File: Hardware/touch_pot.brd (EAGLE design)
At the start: 44.5 x 78.7 mm, 78 parts, among them U1 PIC16F1829, U2 AD5262, U3 5V

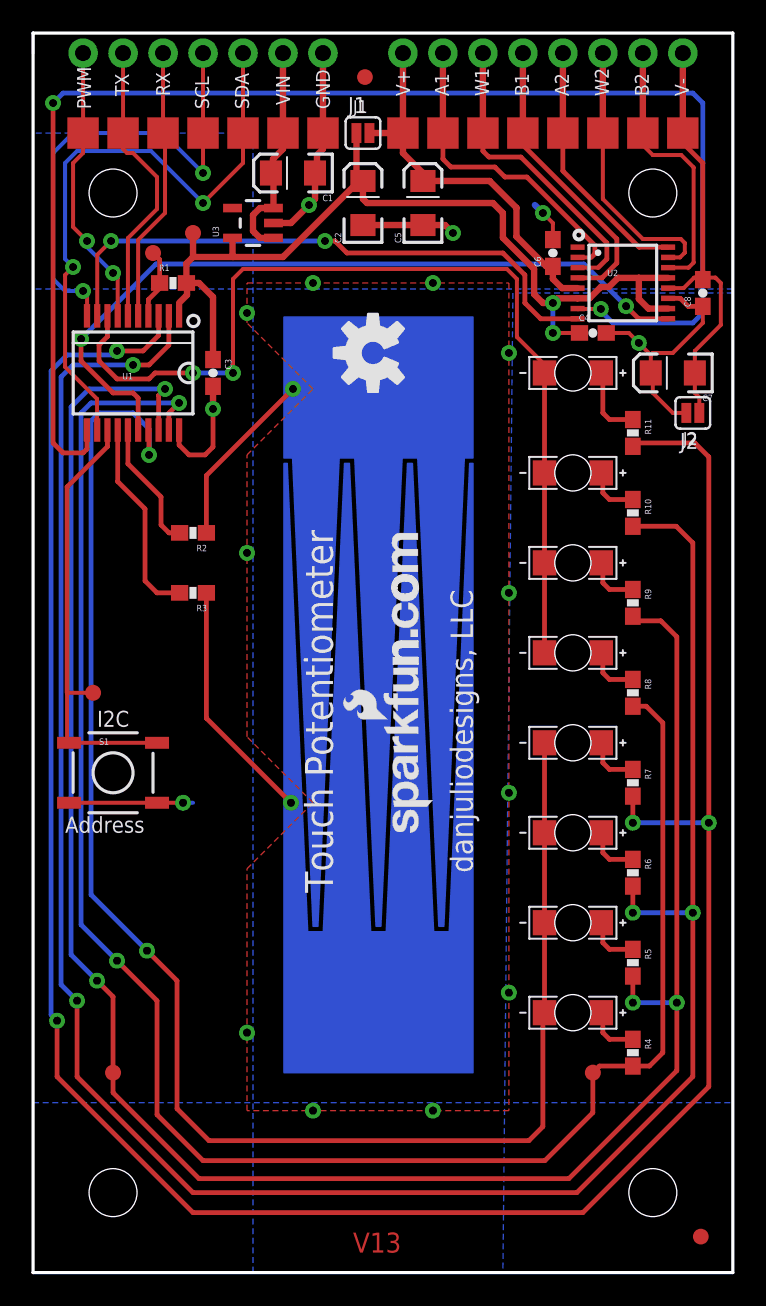
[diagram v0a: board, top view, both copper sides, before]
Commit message: Clean-up, change button text
Moved traces away from hole, deleted unused ground traces, resized one
trace, changed button text for both i2c and cal.
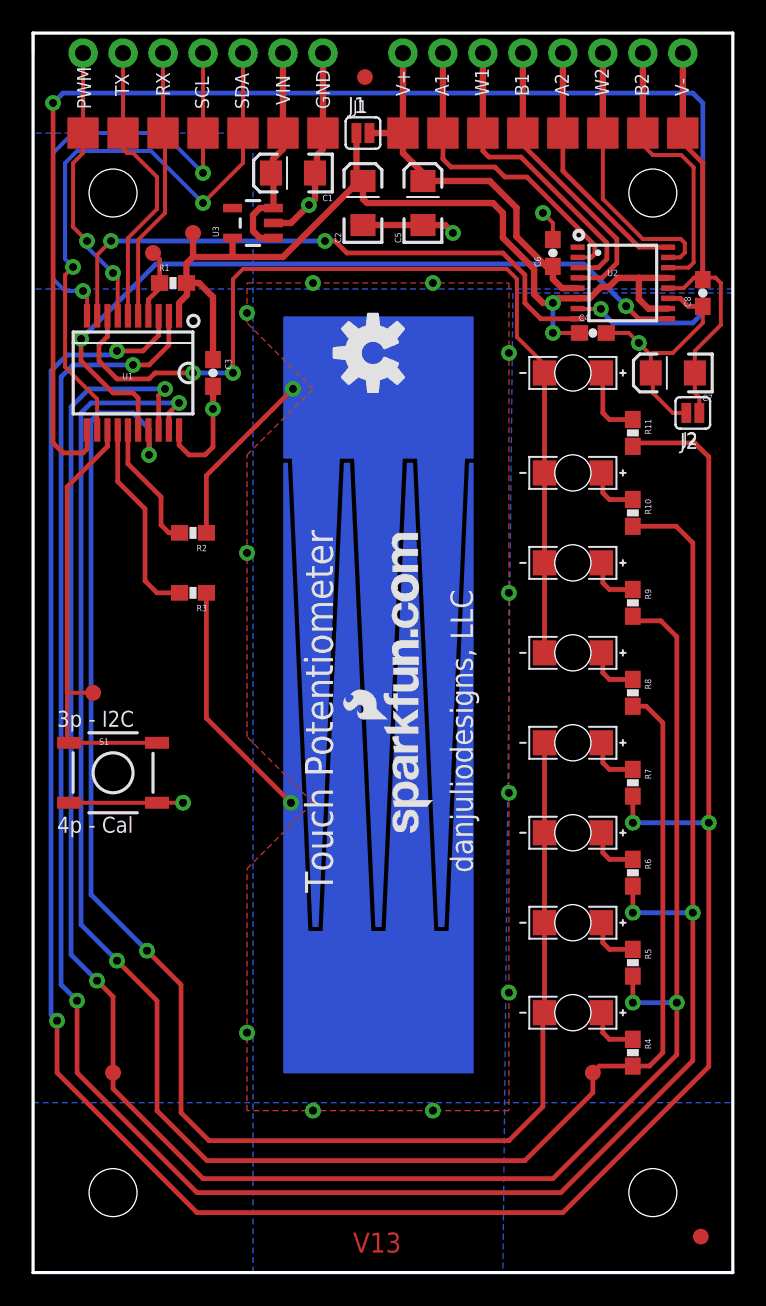
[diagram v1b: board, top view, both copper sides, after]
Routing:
- net GND: track 52.9 -> 51.6 mm
- net LA3: track 154.1 -> 153.2 mm
- net LA0: track 116.0 -> 115.1 mm
- net LA1: track 130.2 -> 129.5 mm
- net LED_PWM1: track 102.4 -> 101.6 mm
- net LA2: track 143.3 -> 142.5 mm
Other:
- board text added: "3p - I2C"
- board text added: "4p - Cal"
- board text removed: "Address"
- board text removed: "I2C"
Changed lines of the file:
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@@
 <text x="53.34" y="-16.51" size="1.778" layer="51" font="vector" ratio="10">danjuliodesigns, LLC</text>
 <text x="20.32" y="1.27" size="1.27" layer="1" font="vector" ratio="15" distance="45">V13</text>
-<text x="4.064" y="34.671" size="1.016" layer="21" font="vector" ratio="15">I2C</text>
-<text x="2.032" y="27.94" size="1.016" layer="21" font="vector" ratio="15">Address</text>
+<text x="1.524" y="34.671" size="1.016" layer="21" font="vector" ratio="15">3p - I2C</text>
+<text x="1.524" y="27.94" size="1.016" layer="21" font="vector" ratio="15">4p - Cal</text>
 <text x="20.32" y="73.66" size="0.8128" layer="21" font="vector" ratio="15">J1</text>
 <text x="41.275" y="52.578" size="0.8128" layer="21" font="vector" ratio="15">J2</text>
@@
 <wire x1="35.9" y1="63.84" x2="36.449" y2="64.389" width="0.3048" layer="1"/>
 <contactref element="U2" pad="3"/>
-<wire x1="35.9" y1="63.84" x2="34.59" y2="63.84" width="0.254" layer="1"/>
+<wire x1="35.9" y1="63.84" x2="34.59" y2="63.84" width="0.3048" layer="1"/>
 <wire x1="28.575" y1="72.39" x2="28.575" y2="71.247" width="0.3048" layer="1"/>
 <wire x1="28.575" y1="71.247" x2="28.956" y2="70.866" width="0.3048" layer="1"/>
@@
 <contactref element="C6" pad="2"/>
 <via x="32.385" y="67.31" extent="1-16" drill="0.508"/>
-<wire x1="32.385" y1="67.31" x2="31.877" y2="67.818" width="0.4064" layer="16"/>
 <contactref element="C8" pad="1"/>
 <wire x1="40.34" y1="61.89" x2="41.107" y2="61.89" width="0.3048" layer="1"/>
@@
 <wire x1="2.286" y1="29.845" x2="9.525" y2="29.845" width="0.254" layer="1"/>
 <via x="9.525" y="29.845" extent="1-16" drill="0.508"/>
-<wire x1="9.525" y1="29.845" x2="10.16" y2="29.845" width="0.254" layer="16"/>
 <wire x1="33.02" y1="65.62" x2="33.02" y2="66.675" width="0.254" layer="1"/>
 <wire x1="33.02" y1="66.675" x2="32.385" y2="67.31" width="0.254" layer="1"/>
@@
 <wire x1="1.778" y1="18.288" x2="1.778" y2="56.896" width="0.3048" layer="16"/>
 <wire x1="2.794" y1="17.272" x2="1.778" y2="18.288" width="0.3048" layer="16"/>
-<wire x1="2.794" y1="12.446" x2="2.794" y2="17.272" width="0.3048" layer="1"/>
-<wire x1="10.16" y1="5.08" x2="2.794" y2="12.446" width="0.3048" layer="1"/>
-<wire x1="10.16" y1="5.08" x2="34.544" y2="5.08" width="0.3048" layer="1"/>
-<wire x1="34.544" y1="5.08" x2="41.91" y2="12.446" width="0.3048" layer="1"/>
+<wire x1="2.794" y1="12.7" x2="2.794" y2="17.272" width="0.3048" layer="1"/>
+<wire x1="10.414" y1="5.08" x2="2.794" y2="12.7" width="0.3048" layer="1"/>
+<wire x1="10.414" y1="5.08" x2="33.528" y2="5.08" width="0.3048" layer="1"/>
+<wire x1="33.528" y1="5.08" x2="41.91" y2="13.462" width="0.3048" layer="1"/>
 <wire x1="2.54" y1="57.658" x2="6.35" y2="57.658" width="0.3048" layer="16"/>
 <wire x1="41.91" y1="22.86" x2="38.1" y2="22.86" width="0.3048" layer="16"/>
-<wire x1="41.91" y1="12.446" x2="41.91" y2="22.86" width="0.3048" layer="1"/>
+<wire x1="41.91" y1="13.462" x2="41.91" y2="22.86" width="0.3048" layer="1"/>
 <wire x1="41.91" y1="22.86" x2="41.91" y2="46.355" width="0.3048" layer="1"/>
 <wire x1="41.91" y1="46.355" x2="40.855" y2="47.41" width="0.3048" layer="1"/>
@@
 <wire x1="1.143" y1="16.383" x2="1.143" y2="57.277" width="0.3048" layer="16"/>
 <wire x1="1.524" y1="16.002" x2="1.143" y2="16.383" width="0.3048" layer="16"/>
-<wire x1="42.926" y1="11.811" x2="42.926" y2="28.575" width="0.3048" layer="1"/>
+<wire x1="42.926" y1="13.081" x2="42.926" y2="28.575" width="0.3048" layer="1"/>
 <wire x1="42.926" y1="28.575" x2="42.926" y2="51.816" width="0.3048" layer="1"/>
 <wire x1="42.926" y1="51.816" x2="42.037" y2="52.705" width="0.3048" layer="1"/>
@@
 <via x="38.1" y="28.575" extent="1-16" drill="0.508"/>
 <via x="42.926" y="28.575" extent="1-16" drill="0.508"/>
-<wire x1="42.926" y1="11.811" x2="34.925" y2="3.81" width="0.3048" layer="1"/>
-<wire x1="34.925" y1="3.81" x2="10.16" y2="3.81" width="0.3048" layer="1"/>
-<wire x1="10.16" y1="3.81" x2="1.524" y2="12.446" width="0.3048" layer="1"/>
-<wire x1="1.524" y1="12.446" x2="1.524" y2="16.002" width="0.3048" layer="1"/>
+<wire x1="42.926" y1="13.081" x2="33.655" y2="3.81" width="0.3048" layer="1"/>
+<wire x1="33.655" y1="3.81" x2="10.414" y2="3.81" width="0.3048" layer="1"/>
+<wire x1="10.414" y1="3.81" x2="1.524" y2="12.7" width="0.3048" layer="1"/>
+<wire x1="1.524" y1="12.7" x2="1.524" y2="16.002" width="0.3048" layer="1"/>
 <contactref element="R7" pad="2"/>
 <contactref element="R11" pad="2"/>
@@
 <wire x1="3.683" y1="24.003" x2="3.683" y2="54.102" width="0.3048" layer="16"/>
 <wire x1="7.239" y1="20.447" x2="3.683" y2="24.003" width="0.3048" layer="16"/>
-<wire x1="9.144" y1="10.414" x2="9.144" y2="18.542" width="0.3048" layer="1"/>
-<wire x1="9.144" y1="18.542" x2="7.239" y2="20.447" width="0.3048" layer="1"/>
-<wire x1="11.176" y1="8.382" x2="9.144" y2="10.414" width="0.3048" layer="1"/>
-<wire x1="11.176" y1="8.382" x2="31.496" y2="8.382" width="0.3048" layer="1"/>
-<wire x1="31.496" y1="8.382" x2="32.385" y2="9.271" width="0.3048" layer="1"/>
+<wire x1="9.398" y1="10.16" x2="9.398" y2="18.288" width="0.3048" layer="1"/>
+<wire x1="9.398" y1="18.288" x2="7.239" y2="20.447" width="0.3048" layer="1"/>
+<wire x1="11.176" y1="8.382" x2="9.398" y2="10.16" width="0.3048" layer="1"/>
+<wire x1="11.176" y1="8.382" x2="30.226" y2="8.382" width="0.3048" layer="1"/>
+<wire x1="30.226" y1="8.382" x2="32.385" y2="10.541" width="0.3048" layer="1"/>
 <via x="7.366" y="51.943" extent="1-16" drill="0.508"/>
 <via x="7.239" y="20.447" extent="1-16" drill="0.508"/>
 <contactref element="D1" pad="C"/>
-<wire x1="32.385" y1="9.271" x2="32.385" y2="16.405" width="0.3048" layer="1"/>
+<wire x1="32.385" y1="10.541" x2="32.385" y2="16.405" width="0.3048" layer="1"/>
 <wire x1="32.385" y1="16.405" x2="32.49" y2="16.51" width="0.3048" layer="1"/>
 <contactref element="D2" pad="C"/>
@@
 <wire x1="4.064" y1="18.542" x2="2.413" y2="20.193" width="0.3048" layer="16"/>
 <wire x1="40.894" y1="17.145" x2="38.1" y2="17.145" width="0.3048" layer="16"/>
-<wire x1="40.894" y1="12.827" x2="40.894" y2="17.145" width="0.3048" layer="1"/>
+<wire x1="40.894" y1="13.843" x2="40.894" y2="17.145" width="0.3048" layer="1"/>
 <wire x1="40.894" y1="17.145" x2="40.894" y2="40.386" width="0.3048" layer="1"/>
 <wire x1="40.894" y1="40.386" x2="39.878" y2="41.402" width="0.3048" layer="1"/>
@@
 <wire x1="38.293" y1="41.402" x2="38.293" y2="41.502" width="0.3048" layer="1"/>
 <contactref element="TP5" pad="P$1"/>
-<wire x1="5.08" y1="11.43" x2="5.08" y2="12.7" width="0.3048" layer="1"/>
+<wire x1="5.08" y1="11.684" x2="5.08" y2="12.7" width="0.3048" layer="1"/>
 <wire x1="4.064" y1="18.542" x2="5.08" y2="17.526" width="0.3048" layer="1"/>
 <wire x1="5.08" y1="17.526" x2="5.08" y2="12.7" width="0.3048" layer="1"/>
-<wire x1="10.541" y1="5.969" x2="5.08" y2="11.43" width="0.3048" layer="1"/>
-<wire x1="10.541" y1="5.969" x2="34.036" y2="5.969" width="0.3048" layer="1"/>
-<wire x1="34.036" y1="5.969" x2="40.894" y2="12.827" width="0.3048" layer="1"/>
+<wire x1="10.795" y1="5.969" x2="5.08" y2="11.684" width="0.3048" layer="1"/>
+<wire x1="10.795" y1="5.969" x2="33.02" y2="5.969" width="0.3048" layer="1"/>
+<wire x1="33.02" y1="5.969" x2="40.894" y2="13.843" width="0.3048" layer="1"/>
 <contactref element="R5" pad="2"/>
 <contactref element="R9" pad="2"/>
@@
 <wire x1="3.048" y1="22.098" x2="3.048" y2="54.61" width="0.3048" layer="16"/>
 <wire x1="5.334" y1="19.812" x2="3.048" y2="22.098" width="0.3048" layer="16"/>
-<wire x1="7.874" y1="10.033" x2="7.874" y2="17.272" width="0.3048" layer="1"/>
+<wire x1="7.874" y1="10.287" x2="7.874" y2="17.272" width="0.3048" layer="1"/>
 <wire x1="7.874" y1="17.272" x2="5.334" y2="19.812" width="0.3048" layer="1"/>
-<wire x1="10.795" y1="7.112" x2="7.874" y2="10.033" width="0.3048" layer="1"/>
-<wire x1="10.795" y1="7.112" x2="32.512" y2="7.112" width="0.3048" layer="1"/>
-<wire x1="32.512" y1="7.112" x2="35.56" y2="10.16" width="0.3048" layer="1"/>
+<wire x1="11.049" y1="7.112" x2="7.874" y2="10.287" width="0.3048" layer="1"/>
+<wire x1="11.049" y1="7.112" x2="31.242" y2="7.112" width="0.3048" layer="1"/>
+<wire x1="31.242" y1="7.112" x2="35.56" y2="11.43" width="0.3048" layer="1"/>
 <via x="9.271" y="55.245" extent="1-16" drill="0.508"/>
 <via x="5.334" y="19.812" extent="1-16" drill="0.508"/>
 <contactref element="TP4" pad="P$1"/>
-<wire x1="35.56" y1="10.16" x2="35.56" y2="12.7" width="0.3048" layer="1"/>
+<wire x1="35.56" y1="11.43" x2="35.56" y2="12.7" width="0.3048" layer="1"/>
 <contactref element="R4" pad="2"/>
 <contactref element="R8" pad="2"/>

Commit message: Last QC Check changes
Minor changes based on QC Checklist.
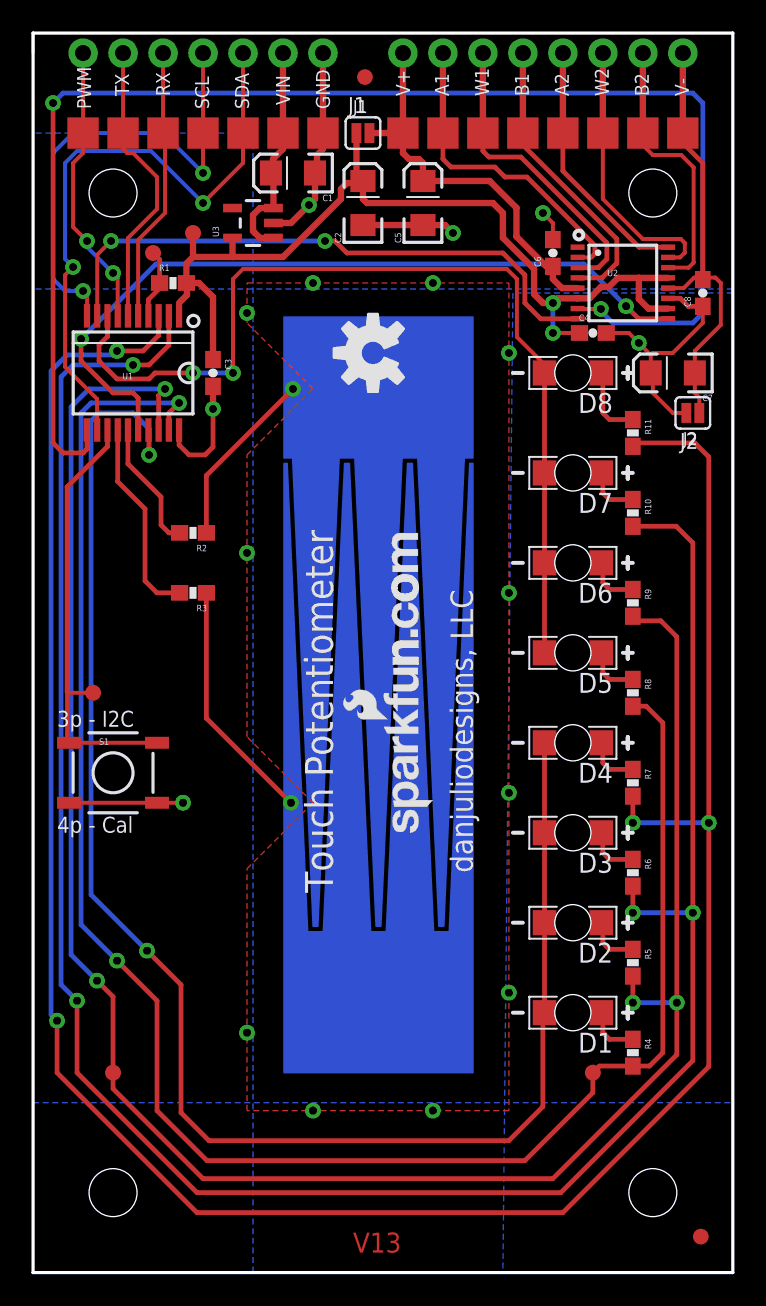
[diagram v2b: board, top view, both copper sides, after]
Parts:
- renumbered CON1 to TP6, CON10 to TP15, CON11 to TP16, CON12 to TP17, CON13 to TP18, CON14 to TP19, CON15 to TP20, CON2 to TP7, CON3 to TP8, CON4 to TP9, CON5 to TP10, CON6 to TP11, CON7 to TP12, CON8 to TP13, CON9 to TP14
